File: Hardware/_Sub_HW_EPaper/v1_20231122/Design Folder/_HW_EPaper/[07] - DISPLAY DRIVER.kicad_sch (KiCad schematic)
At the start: 0 parts

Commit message: EPaper schematic is almost done...
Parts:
- added C701: 100nF_50V, Capacitor_SMD:C_0402_1005Metric, symbol _SCHLIB_Epaper:CAP_100nF_50V_X7R_C0402
- added C702, C703, C704, C705, C706, C707, C708, C709, C710: 4u7F_16V, Capacitor_SMD:C_0805_2012Metric, symbol _SCHLIB_Epaper:CAP_4.7uF_16V_X7R_C0805
- added D701, D702, D703: SS2040FL, Diode_SMD:D_SOD-123F, symbol _SCHLIB_Epaper:DIODE_SCHOTTKY _SS2040FL_R1_00001_40V_2A_S0D-123FL
- added J701: FPC_24POS_BOTTOM_0.5P, Connector_FFC-FPC:Hirose_FH12-24S-0.5SH_1x24-1MP_P0.50mm_Horizontal, symbol _SCHLIB_Epaper:CONN_FPC_24POS_0.5P_BOTTOM_CF35242D0RD-NH_RA
- added L701: 10uH_600mA, symbol _SCHLIB_Epaper:IND_10uH_600mA_413mOhm_SMD (3.8X3.8)
- added Q701: AS3400, Package_TO_SOT_SMD:SOT-23-3, symbol _SCHLIB_Epaper:Q_N-CH_AS3400_30A_2A_SOT-23
- added R701: 0.47R_1/8W_5%, Resistor_SMD:R_0805_2012Metric, symbol _SCHLIB_Epaper:RES_0.47R_1/18W_5%_R0805
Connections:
- new net: C706.1, D702.2, L701.2, Q701.3
- new net: C706.2, D701.2, D703.1
- new net E24_BUSY: J701.9
- new net E24_DC: J701.11
- new net E24_GDR: J701.2, Q701.1
- new net E24_RESE: J701.3, Q701.2, R701.1
- new net E24_RST: J701.10
- new net E24_VCOM: C703.1, J701.24
- new net E24_VDD: C710.1, J701.18
- new net E24_VDH: C708.1, J701.20
- new net E24_VDHR: C702.1, J701.5
- new net E24_VDL: C709.1, J701.22
- new net E24_VGH: C707.1, D702.1, J701.21
- new net E24_VGL: C705.1, D703.2, J701.23
- new net E24_~{CS}: J701.12
- new net GND: C701.2, C702.2, C703.2, C704.2, C705.2, C707.2, C708.2, C709.2, C710.2, D701.1, J701.17, J701.8, R701.2
- new net SPI_CLK: J701.13
- new net SPI_SDO: J701.14
- new net VIN: C701.1, C704.1, J701.15, J701.16, L701.1
- no-connect marks 0 -> 5
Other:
- note added: "it must be double checked with the SCHEMATIC"

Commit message: Latest update
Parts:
- added Q1001: SSM3J117TU,LF, _PCBLIB_Epaper:UFM_TOS, symbol _SCHLIB_Epaper:Q_P-Channel_30V_2A_SSM3J117TU,LF_UFM
- added R1001: 10kR_1/16W_1%, Resistor_SMD:R_0402_1005Metric, symbol _SCHLIB_Epaper:RES_10kR_1/16W_1%_R0402
- L701: footprint (none) -> _PCBLIB_Epaper:IND_CDRH3D11HPNP-100NC_SUM
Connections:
- net GND: now also R1001.2
- net PWR: now also Q1001.1, R1001.1
- net VIN: now also Q1001.2; no longer C701.1, C704.1, J701.15, J701.16, L701.1
- new net: C701.1, C704.1, J701.15, J701.16, L701.1, Q1001.3
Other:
- moved on the sheet: C701, C702, C703, C704, C705, C706, C707, C708, C709, C710, D701, D702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

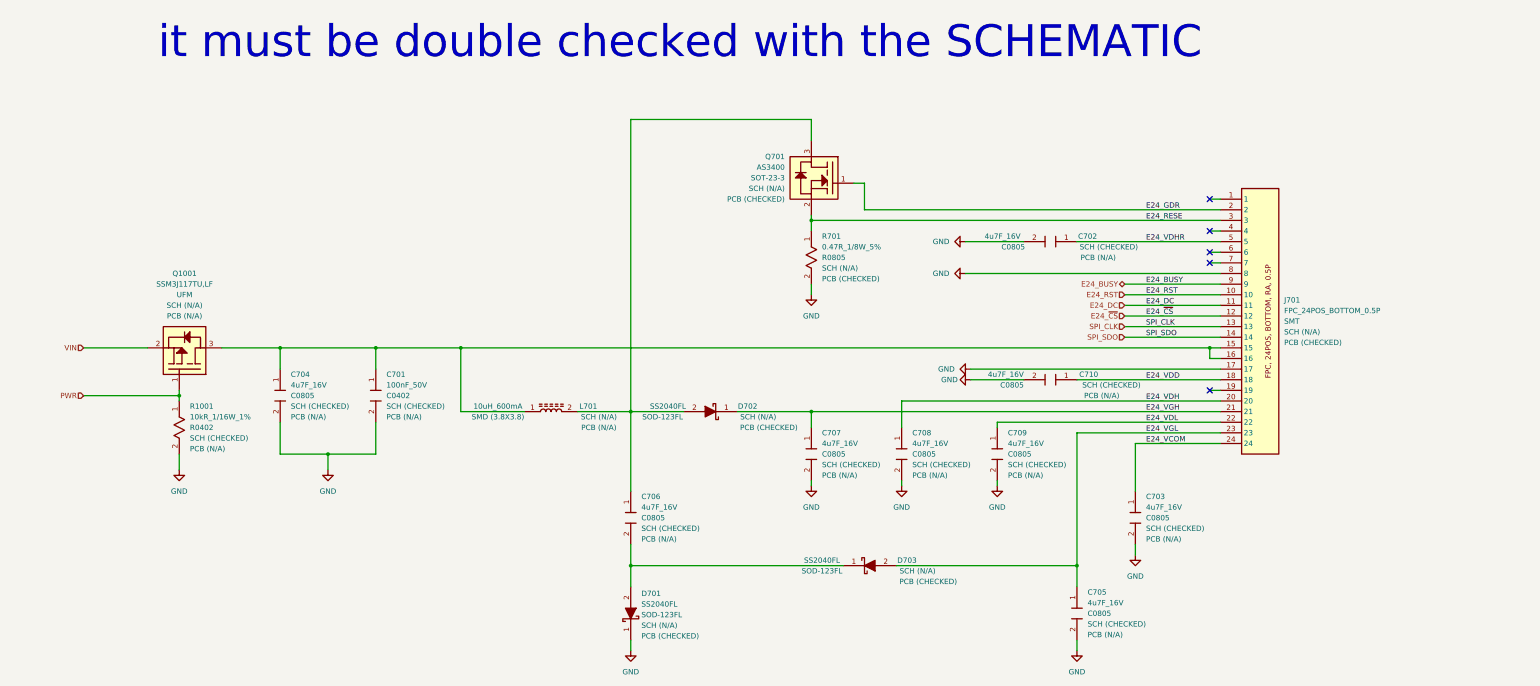
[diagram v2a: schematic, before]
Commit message: Working on epaper hardware
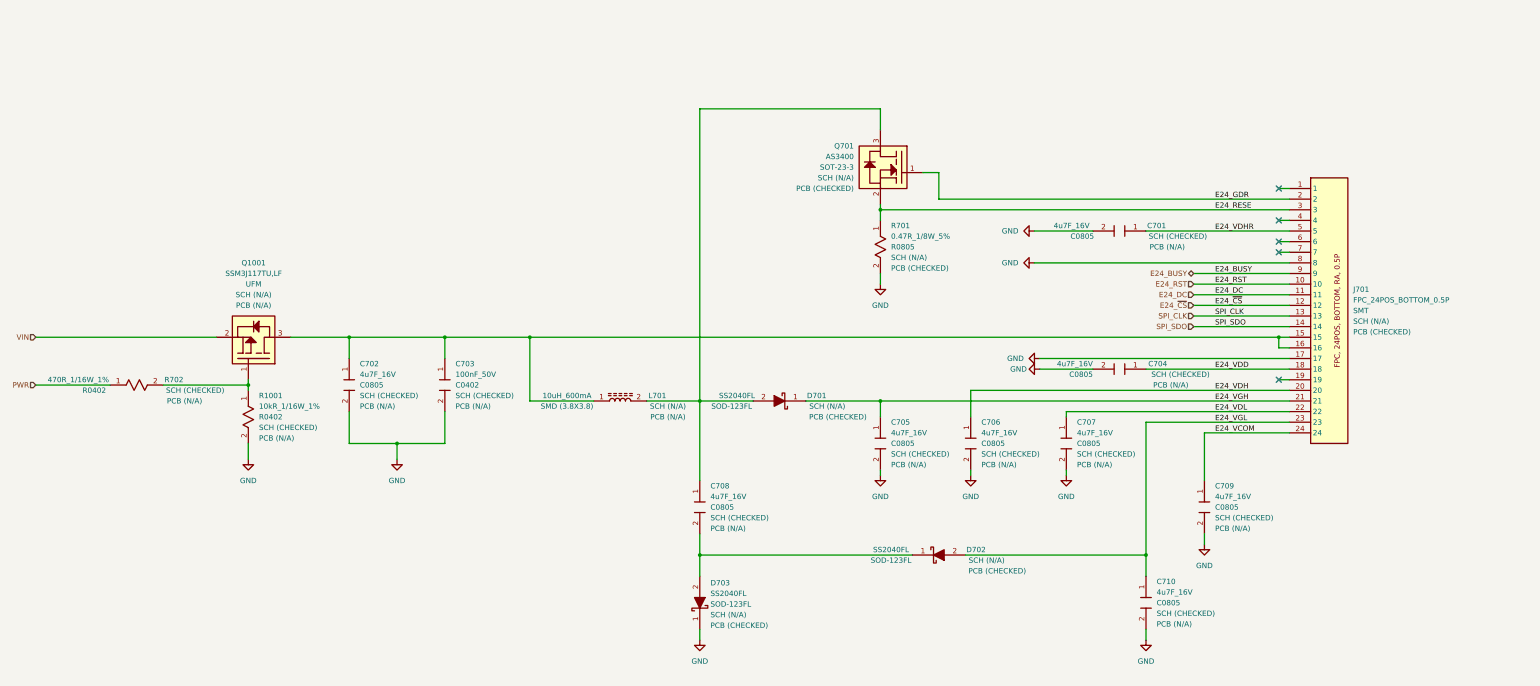
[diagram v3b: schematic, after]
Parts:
- added R702: 470R_1/16W_1%, Resistor_SMD:R_0402_1005Metric, symbol _SCHLIB_Epaper:RES_470R_1/16W_1%_R0402
- renumbered C702 to C701, C704 to C702, C701 to C703, C710 to C704, C707 to C705, C708 to C706, C709 to C707, C706 to C708, C703 to C709, C705 to C710, D702 to D701, D703 to D702, D701 to D703
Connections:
- net PWR: now also R702.1; no longer Q1001.1, R1001.1
- new net: Q1001.1, R1001.1, R702.2
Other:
- note removed: "it must be double checked with the SCHEMATIC"
- moved on the sheet: C701, C702, C703, C704, C705, C706, C707, C708, C709, C710, D701, D702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

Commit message: Hardware is almost done
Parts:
- Q701: footprint Package_TO_SOT_SMD:SOT-23-3 -> Package_TO_SOT_SMD:SOT-23; SCH CHECK SCH (N/A) -> SCH (CHECKED)
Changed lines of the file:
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@@
       (effects (font (size 1.27 1.27)) (justify left))
     )
-    (property "Footprint" "Package_TO_SOT_SMD:SOT-23-3" (at 251.46 62.23 0)
+    (property "Footprint" "Package_TO_SOT_SMD:SOT-23" (at 251.46 62.23 0)
       (effects (font (size 1.27 1.27)) (justify left) hide)
     )
@@
       (effects (font (size 1.27 1.27)) (justify left))
     )
-    (property "SCH CHECK" "SCH (N/A)" (at 237.49 88.9 0)
+    (property "SCH CHECK" "SCH (CHECKED)" (at 237.49 88.9 0)
       (effects (font (size 1.27 1.27)) (justify left))
     )

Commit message: Updating file templates and structures...
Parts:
- C701, C702, C704, C705, C706, C707, C708, C709, C710: Manufacturer (none) -> Murata Electronics; Part Number GRM21BR71C475KE51L -> (none); Part Number (Manufacturer) (none) -> GRM21BR71C475KE51L; Part Number (Vendor) (none) -> 490-14466-2-ND; Vendor (none) -> Digikey
- C703: Manufacturer (none) -> Murata Electronics; Part Number GRM155R71H104KE14J -> (none); Part Number (Manufacturer) (none) -> GRM155R71H104KE14J; Part Number (Vendor) (none) -> 490-13342-2-ND; Vendor (none) -> Digikey
- D701, D702, D703: Manufacturer (none) -> Panjit International Inc.; Part Number SS2040FL_R1_00001 -> (none); Part Number (Manufacturer) (none) -> SS2040FL_R1_00001; Part Number (Vendor) (none) -> 3757-SS2040FL_R1_00001TR-ND; Vendor (none) -> Digikey
- J701: Manufacturer (none) -> Cvilux USA; Part Number CF35242D0RD-NH -> (none); Part Number (Manufacturer) (none) -> CF35242D0RD-NH; Part Number (Vendor) (none) -> 2987-CF35242D0RD-NHTR-ND; Vendor (none) -> Digikey
- L701: Manufacturer (none) -> Sumida America Components Inc.; Part Number CDRH3D11HPNP-100NC -> (none); Part Number (Manufacturer) (none) -> CDRH3D11HPNP-100NC; Part Number (Vendor) (none) -> 308-1966-2-ND; Vendor (none) -> Digikey
- Q1001: Manufacturer (none) -> Toshiba Semiconductor and Storage; Part Number SSM3J117TU,LF -> (none); Part Number (Manufacturer) (none) -> SSM3J117TU,LF; Part Number (Vendor) (none) -> SSM3J117TULFTR-ND; Vendor (none) -> Digikey
- Q701: Manufacturer (none) -> ANBON SEMICONDUCTOR (INT'L) LIMITED; Part Number AS3400 -> (none); Part Number (Manufacturer) (none) -> AS3400; Part Number (Vendor) (none) -> 4530-AS3400TR-ND; Vendor (none) -> Digikey
- R1001: Manufacturer (none) -> Bourns Inc.; Part Number CR0402-FX-1002GLF -> (none); Part Number (Manufacturer) (none) -> CR0402-FX-1002GLF; Part Number (Vendor) (none) -> CR0402-FX-1002GLFTR-ND; Vendor (none) -> Digikey
- R701: Manufacturer (none) -> CTS Resistor Products; Part Number 73L3R47J -> (none); Part Number (Manufacturer) (none) -> 73L3R47J; Part Number (Vendor) (none) -> 73L3R47JTR-ND; Vendor (none) -> Digikey
- R702: Manufacturer (none) -> Bourns Inc.; Part Number CR0402-FX-4700GLF -> (none); Part Number (Manufacturer) (none) -> CR0402-FX-4700GLF; Part Number (Vendor) (none) -> CR0402-FX-4700GLFTR-ND; Vendor (none) -> Digikey
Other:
- moved on the sheet: C701, C702, C703, C704, C705, C706, C707, C708, C709, C710, D701, D702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
